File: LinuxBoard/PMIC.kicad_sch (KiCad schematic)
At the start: 45 parts, among them J6 USB_B_Micro, J7 Barrel_Jack_Switch, SW5 SW_Push, U4 STPMIC1APQR

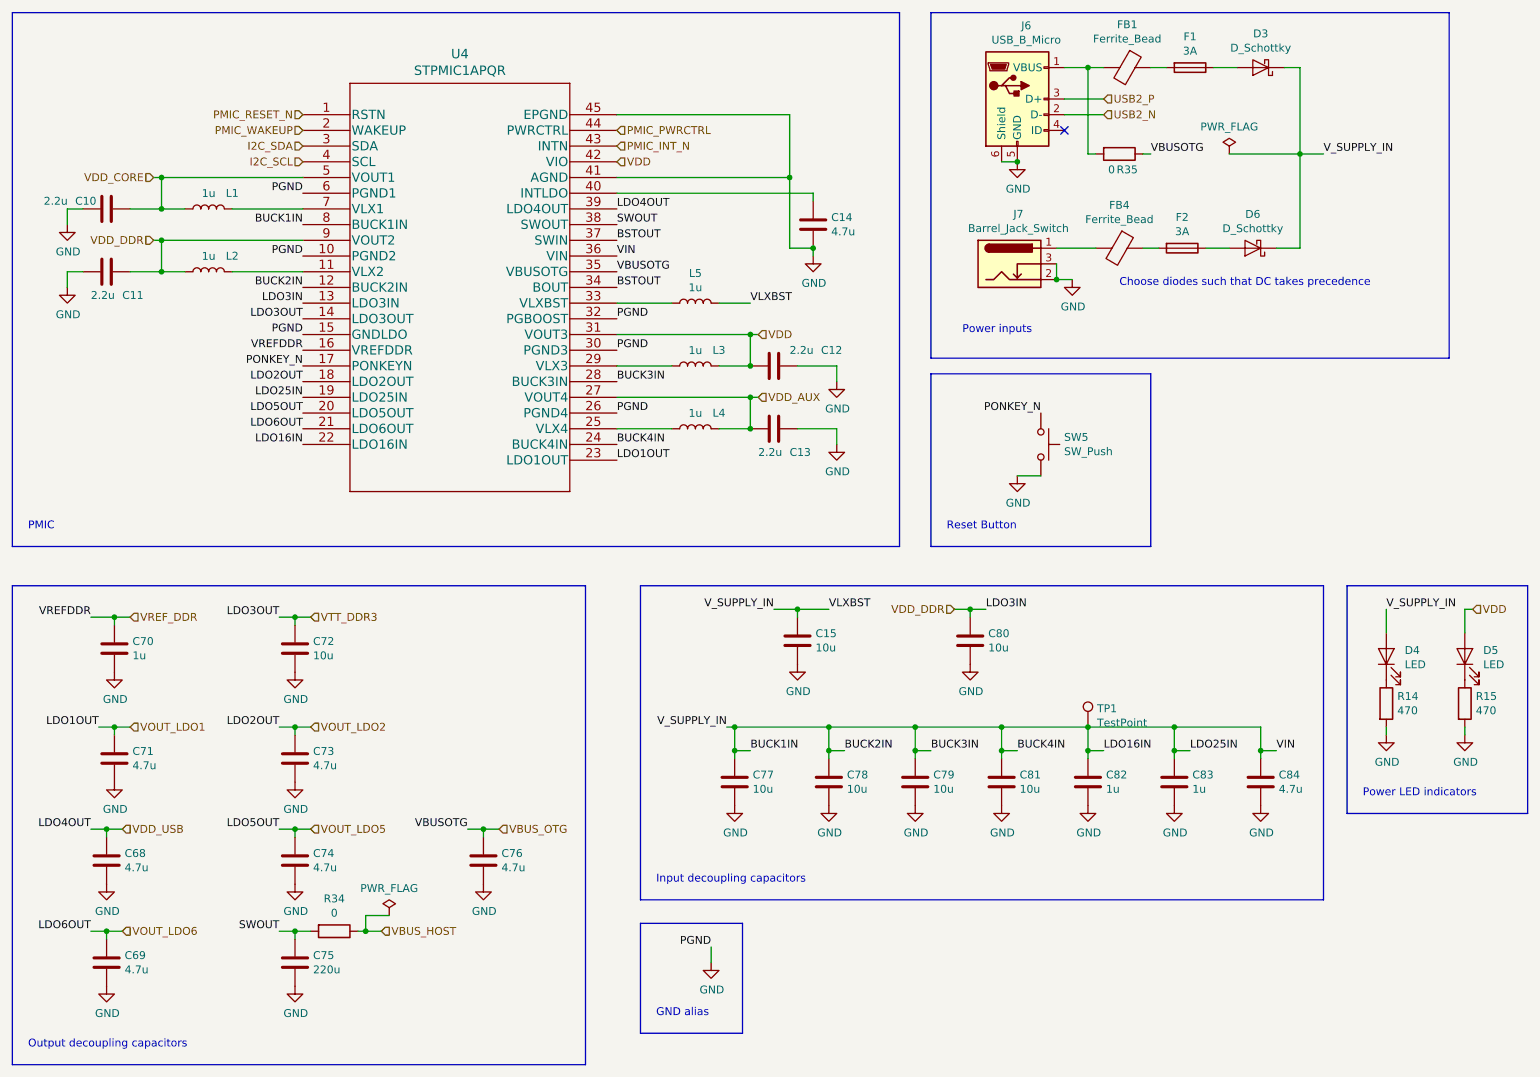
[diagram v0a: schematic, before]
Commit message: Fix ERC errors and reorganize directory
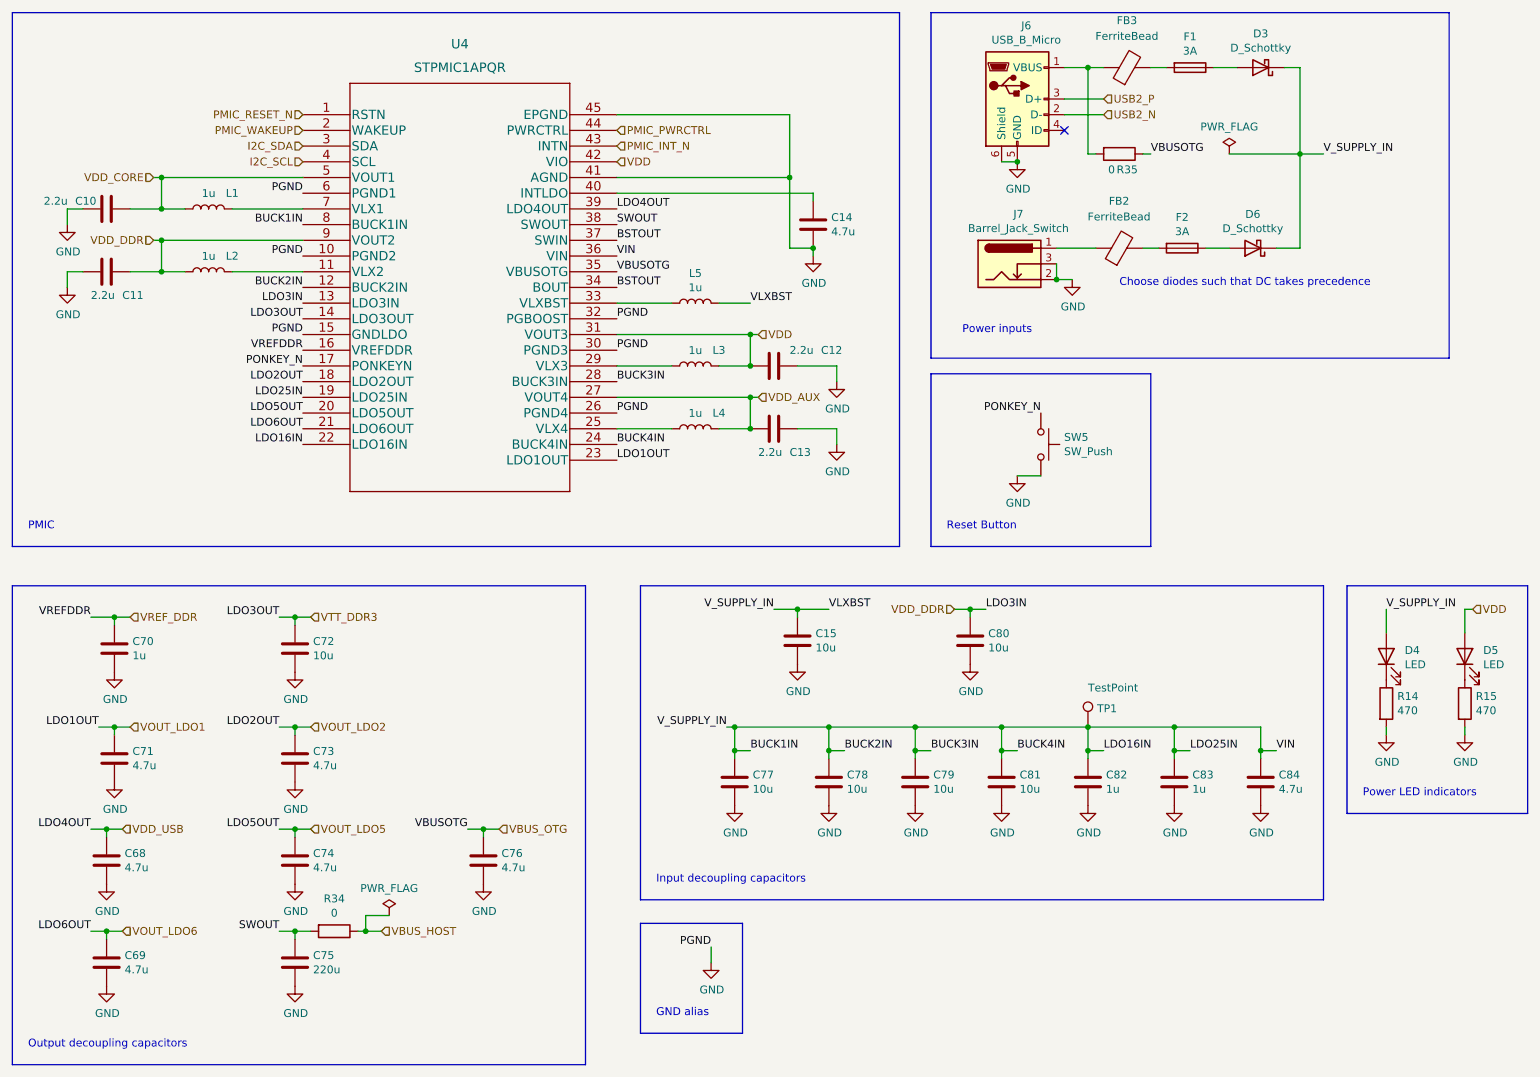
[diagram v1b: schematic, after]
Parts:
- removed FB1, FB4: Ferrite_Bead, Inductor_SMD:L_0603_1608Metric, symbol Device:Ferrite_Bead
- added FB2, FB3: FerriteBead, Inductor_SMD:L_0603_1608Metric_Pad1.05x0.95mm_HandSolder, symbol Device:FerriteBead
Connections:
- net at J6.1 (VBUS), R35.2: now also FB3.1
- net at F1.2: now also FB3.2
- net at J7.1: now also FB2.1
- net at F2.2: now also FB2.2

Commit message: Fix resistor footprints, restart layout
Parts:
- R14, R15, R34, R35: footprint Resistor_SMD:R_0603_1608Metric_Pad1.05x0.95mm_HandSolder -> Resistor_SMD:R_0603_1608Metric_Pad0.98x0.95mm_HandSolder
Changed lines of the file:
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@@
       (effects (font (size 1.27 1.27)) (justify left))
     )
-    (property "Footprint" "Resistor_SMD:R_0603_1608Metric_Pad1.05x0.95mm_HandSolder" (id 2) (at 248.412 130.81 90)
+    (property "Footprint" "Resistor_SMD:R_0603_1608Metric_Pad0.98x0.95mm_HandSolder" (id 2) (at 248.412 130.81 90)
       (effects (font (size 1.27 1.27)) hide)
     )
@@
     (property "Reference" "R34" (id 0) (at 80.01 162.3822 90))
     (property "Value" "0" (id 1) (at 80.01 164.6936 90))
-    (property "Footprint" "Resistor_SMD:R_0603_1608Metric_Pad1.05x0.95mm_HandSolder" (id 2) (at 80.01 165.862 90)
+    (property "Footprint" "Resistor_SMD:R_0603_1608Metric_Pad0.98x0.95mm_HandSolder" (id 2) (at 80.01 165.862 90)
       (effects (font (size 1.27 1.27)) hide)
     )
@@
       (effects (font (size 1.27 1.27)) (justify left))
     )
-    (property "Footprint" "Resistor_SMD:R_0603_1608Metric_Pad1.05x0.95mm_HandSolder" (id 2) (at 261.112 130.81 90)
+    (property "Footprint" "Resistor_SMD:R_0603_1608Metric_Pad0.98x0.95mm_HandSolder" (id 2) (at 261.112 130.81 90)
       (effects (font (size 1.27 1.27)) hide)
     )
@@
     (property "Reference" "R35" (id 0) (at 208.28 44.45 90))
     (property "Value" "0" (id 1) (at 205.74 44.45 90))
-    (property "Footprint" "Resistor_SMD:R_0603_1608Metric_Pad1.05x0.95mm_HandSolder" (id 2) (at 207.01 40.132 90)
-      (effects (font (size 1.27 1.27)) hide)
-    )
+    (property "Footprint" "Resistor_SMD:R_0603_1608Metric_Pad0.98x0.95mm_HandSolder" (id 2) (at 207.01 40.132 90)
+      (effects (font (size 1.27 1.27)) hide)
+    )
